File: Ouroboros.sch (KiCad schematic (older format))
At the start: 132 parts, among them J1 E1_3.5mm, J10 E1_3.5mm, J11 E1_3.5mm, J12 PWR_IN_PHNX, J13 PWR_IN_PHNX, J14 PWR_IN_PHNX, J15 PWR_IN_PHNX, J16 E1_3.5mm, J2 E1_3.5mm, J3 E1_3.5mm, J4 E1_3.5mm, J5 E1_3.5mm, J6 E1_3.5mm, J7 E1_3.5mm, J8 E1_3.5mm, J9 E1_3.5mm, SW1 SW_SPDT, U1 CD4017, U10 LM324, U11 LM324, U12 LM324, U13 LM324, U14 LM324, U15 NE555, U2 CD4017, U3 CD4017, U4 CD4017, U5 CD4017, U6 CD4017, U7 CD4017, U8 CD4017, U9 CD4017

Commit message: made schematic
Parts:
- added C?: 0.1uf, symbol Device:C
- added C?: 10uf, Capacitor_THT:CP_Radial_D5.0mm_P2.00mm, symbol Device:CP
- added D? (x19): 1N914, symbol Device:D
- added R? (x11): 10k, HammerheadAudio:R_THT_P7.62, symbol Device:R
- added R?: 10k, symbol Device:R
- added R?: 1k, HammerheadAudio:R_THT_P7.62, symbol Device:R
- added U?: CD4048, symbol CD4048:CD4048
- R24: value 1k -> 10k
- R25: value 220 -> 1k
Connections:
- net ALL: now also D?.2 (A), U?.1 (Out); no longer U12.10 (+)
- net GND: now also C?.2, D?.2 (A), R?.1, R?.2, R?.2, R?.2, R?.2, R?.2, R?.2, R?.2, R?.2, R?.2, R?.2, U?.15 (Exp), U?.7 (Kb), U?.8 (Vss), U?.9 (Kc); no longer U9.15 (RES)
- net TRIG_IN: now also R?.2; no longer U10.3 (+)
- net VCC: now also C?.1, U?.10 (Ka), U?.16 (Vdd)
- net VREF: no longer U12.9 (-)
- net at U15.3 (Q): now also R?.1; no longer J16.3 (Pin_3)
- net B2: now reaches R4.2, R5.2, U10.7
- net at U2.15 (RES): now also D?.2 (A); no longer U2.7 (Q3)
- net at U3.10 (Q4): now also D?.1 (K), D?.1 (K), R?.1; no longer U3.15 (RES)
- net at U4.1 (Q5): now also D?.1 (K), D?.1 (K), R?.1; no longer U4.15 (RES)
- net at U5.15 (RES): now also D?.2 (A); no longer U5.5 (Q6)
- net at U6.15 (RES): now also D?.2 (A); no longer U6.6 (Q7)
- net at U7.15 (RES): now also D?.2 (A); no longer U7.9 (Q8)
- net at U8.11 (Q9): now also D?.1 (K), D?.1 (K), R?.1; no longer U8.15 (RES)
- net B5: now reaches R10.2, R11.2, U11.1
- net B6: now reaches R12.2, R13.2, U11.7
- net B7: now reaches R14.2, R15.2, U11.8
- net B8: now reaches R16.2, R17.2, U11.14
- net B9: now reaches R18.2, R19.2, U12.1
- net B10: now reaches R20.2, R21.2, U12.7
- net B10: now also U?.11 (D), U?.12 (C), U?.13 (B), U?.14 (A), U?.2 (Kd), U?.3 (H), U?.4 (G), U?.5 (F), U?.6 (E)
- net at R22.2, R23.2, U12.8: now also U12.9 (-)
- net B3: now reaches R6.2, R7.2, U10.8
- net B4: now reaches R8.2, R9.2, U10.14
- net at U1.15 (RES): now also D?.2 (A); no longer U1.4 (Q2)
- new net: J16.3 (Pin_3), R?.2
- new net: D?.1 (K), R?.1, U10.3 (+)
- new net: D?.1 (K), D?.1 (K), R?.1, U2.7 (Q3)
- new net: D?.2 (A), U3.15 (RES)
- new net: D?.2 (A), U4.15 (RES)
- new net: D?.1 (K), D?.1 (K), R?.1, U5.5 (Q6)
- new net: D?.1 (K), D?.1 (K), R?.1, U6.6 (Q7)
- new net: D?.1 (K), D?.1 (K), R?.1, U7.9 (Q8)
- new net: D?.2 (A), U8.15 (RES)
- new net: D?.1 (K), R?.1, U9.15 (RES)
- new net: C?.1, D?.1 (K), R?.2, U12.10 (+)
- new net: D?.1 (K), D?.1 (K), R?.1, U1.4 (Q2)
- new net RESET: C?.2, D?.2 (A), D?.2 (A), D?.2 (A), D?.2 (A), D?.2 (A), D?.2 (A), D?.2 (A), D?.2 (A), D?.2 (A), R?.1
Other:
- moved on the sheet: D0, D1, D65, J1, J11, J16, R1, R2, R22, R23, R24, R25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

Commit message: cleaned up schematic errors
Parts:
- added SW2: SW_Push, Button_Switch_THT:SW_PUSH_6mm, symbol Switch:SW_Push
- C4: renamed from C?; footprint (none) -> Capacitor_THT:C_Disc_D3.0mm_W2.0mm_P2.50mm
- D0, D1, D2, D3, D4, D5, D6, D7, D8, D9: footprint (none) -> HammerheadAudio:LED_Centered
- D10, D11, D12, D13, D14, D15, D16, D17, D18, D19, D20, D21, D22, D23, D24, D25, D26, D27, D28, D29, D30, D31, D32, D33, D34, D35, D36, D37, D38, D39, D40, D41, D42, D43, D44, D45, D46, D47, D48, D49, D50, D51, D52, D53, D54, D55, D56, D57, D58, D59, D60, D61, D62, D63, D64, D65: footprint (none) -> HammerheadAudio:LED_Centered_NoRef
- D68, D69, D70, D71, D72, D73, D74, D75, D76, D77, D78, D79, D80, D81, D82, D83, D84, D85, D86: renamed from D?; footprint (none) -> HammerheadAudio:DO-35-P5mm
- R29: renamed from R?; footprint (none) -> HammerheadAudio:R_THT_P7.62
- U16: renamed from U?; footprint (none) -> Package_DIP:DIP-16_W7.62mm_Socket
- gave numbers to parts that had none: 13
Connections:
- net B10: no longer U16.11 (D), U16.12 (C), U16.13 (B), U16.14 (A), U16.3 (H), U16.4 (G), U16.5 (F), U16.6 (E)
- net B2: now also U16.11 (D)
- net B3: now also U16.12 (C)
- net B4: now also U16.13 (B)
- net B5: now also U16.14 (A)
- net B6: now also U16.6 (E)
- net B7: now also U16.5 (F)
- net B8: now also U16.4 (G)
- net B9: now also U16.3 (H)
- net DIV10: now also D55.2 (A), U9.3 (Q0)
- net DIV9: no longer D55.2 (A), U9.3 (Q0)
- net GND: now also D11.1 (K)
- net RESET: now also SW2.1
- net VCC: now also SW2.2
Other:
- moved on the sheet: C4, R40

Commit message: cleaned up schematic errors
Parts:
- removed C3: 10uf, Capacitor_THT:CP_Radial_D5.0mm_P2.00mm, symbol Device:CP
- D10: footprint HammerheadAudio:LED_Centered_NoRef -> HammerheadAudio:LED_Centered
- renumbered C4 to C3, C5 to C4, U13 to U11, U14 to U12, U16 to U13, U15 to U14
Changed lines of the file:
@@
 F 0 "D10" H 2493 9445 50  0000 C CNN
 F 1 "LED" H 2493 9536 50  0000 C CNN
-F 2 "HammerheadAudio:LED_Centered_NoRef" H 2500 9700 50  0001 C CNN
+F 2 "HammerheadAudio:LED_Centered" H 2500 9700 50  0001 C CNN
 F 3 "~" H 2500 9700 50  0001 C CNN
 	1    2500 9700
@@
 	950  12650 1000 12650
 $Comp
-L Timer:NE555 U15
+L Timer:NE555 U14
 U 1 1 5E794E13
 P 15650 5550
-F 0 "U15" H 15350 5900 50  0000 C CNN
+F 0 "U14" H 15350 5900 50  0000 C CNN
 F 1 "NE555" H 15900 5900 50  0000 C CNN
 F 2 "Package_DIP:DIP-8_W7.62mm_Socket" H 15650 5550 50  0001 C CNN
@@
 	16150 5750 16150 6100
 Wire Wire Line
-	16150 6300 15250 6300
-Wire Wire Line
 	14850 6300 14850 5350
 Wire Wire Line
@@
 $EndComp
 $Comp
-L Amplifier_Operational:LM324 U13
+L Amplifier_Operational:LM324 U11
 U 5 1 5EA7F911
 P 14900 2000
-F 0 "U13" H 14858 2046 50  0000 L CNN
+F 0 "U11" H 14858 2046 50  0000 L CNN
 F 1 "LM324" H 14858 1955 50  0000 L CNN
 F 2 "Package_DIP:DIP-14_W7.62mm_Socket" H 14850 2100 50  0001 C CNN
@@
 	14400 3750 14650 3750
 $Comp
-L Amplifier_Operational:LM324 U14
+L Amplifier_Operational:LM324 U12
 U 5 1 5E8E8FA2
 P 15350 2000
-F 0 "U14" H 15308 2046 50  0000 L CNN
+F 0 "U12" H 15308 2046 50  0000 L CNN
 F 1 "LM324" H 15308 1955 50  0000 L CNN
 F 2 "Package_DIP:DIP-14_W7.62mm_Socket" H 15300 2100 50  0001 C CNN
@@
 Wire Wire Line
 	15250 2400 15250 2450
-$Comp
-L Device:CP C3
-U 1 1 5E7E848A
-P 15250 6500
-F 0 "C3" H 15368 6546 50  0000 L CNN
-F 1 "10uf" H 15368 6455 50  0000 L CNN
-F 2 "Capacitor_THT:CP_Radial_D5.0mm_P2.00mm" H 15288 6350 50  0001 C CNN
-F 3 "~" H 15250 6500 50  0001 C CNN
-	1    15250 6500
-	1    0    0    -1
-$EndComp
-Wire Wire Line
-	15250 6350 15250 6300
-Connection ~ 15250 6300
-Wire Wire Line
-	15250 6300 14850 6300
-Wire Wire Line
-	14850 6650 14850 6700
-Wire Wire Line
-	15250 6650 15250 6700
-Wire Wire Line
-	15250 6700 14850 6700
-Connection ~ 14850 6700
-Wire Wire Line
-	14850 6700 14850 6750
 Wire Wire Line
 	16150 5350 16550 5350
@@
 	5250 8600 5250 8550
 $Comp
-L Device:C C4
+L Device:C C3
 U 1 1 6155F9DF
 P 5250 7950
-F 0 "C4" H 5365 7996 50  0000 L CNN
+F 0 "C3" H 5365 7996 50  0000 L CNN
 F 1 "0.1uf" H 5365 7905 50  0000 L CNN
 F 2 "Capacitor_THT:C_Disc_D3.0mm_W2.0mm_P2.50mm" H 5288 7800 50  0001 C CNN
@@
 	16950 5350 16850 5350
 $Comp
-L CD4048:CD4048 U16
+L CD4048:CD4048 U13
 U 1 1 61A5E271
 P 8650 8300
-F 0 "U16" H 8650 8565 50  0000 C CNN
+F 0 "U13" H 8650 8565 50  0000 C CNN
 F 1 "CD4048" H 8650 8474 50  0000 C CNN
 F 2 "Package_DIP:DIP-16_W7.62mm_Socket" H 8150 8300 50  0001 C CNN
@@
 $EndComp
 $Comp
-L Device:CP C5
+L Device:CP C4
 U 1 1 624F28D9
 P 1400 10950
-F 0 "C5" H 1518 10996 50  0000 L CNN
+F 0 "C4" H 1518 10996 50  0000 L CNN
 F 1 "10uf" H 1518 10905 50  0000 L CNN
 F 2 "Capacitor_THT:CP_Radial_D5.0mm_P2.00mm" H 1438 10800 50  0001 C CNN
@@
 Wire Wire Line
 	1200 9250 1250 9250
+Wire Wire Line
+	14850 6650 14850 6750
+Wire Wire Line
+	14850 6300 16150 6300
 $EndSCHEMATC

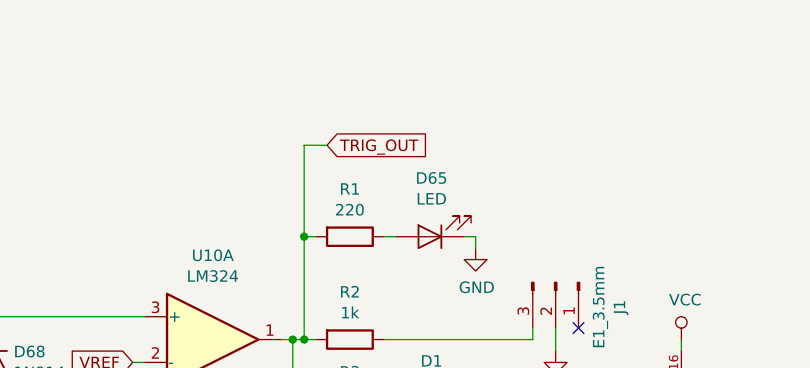
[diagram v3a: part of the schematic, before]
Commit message: added clock in indicator led
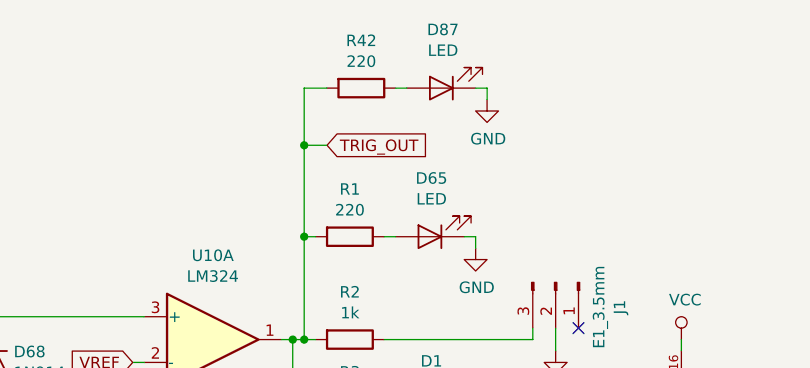
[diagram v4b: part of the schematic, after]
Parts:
- added D87: LED, HammerheadAudio:LED_Centered_NoRef, symbol Device:LED
- added R42: 220, HammerheadAudio:R_THT_P7.62, symbol Device:R
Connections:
- net GND: now also D87.1 (K)
- net TRIG_OUT: now also R42.2
- new net: D87.2 (A), R42.1
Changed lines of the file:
@@
 Wire Wire Line
 	14850 6300 16150 6300
+$Comp
+L Device:LED D87
+U 1 1 5F384FB5
+P 3250 300
+F 0 "D87" H 3243 45  50  0000 C CNN
+F 1 "LED" H 3243 136 50  0000 C CNN
+F 2 "HammerheadAudio:LED_Centered_NoRef" H 3250 300 50  0001 C CNN
+F 3 "~" H 3250 300 50  0001 C CNN
+	1    3250 300
+	-1   0    0    1
+$EndComp
+$Comp
+L power:GND #PWR0119
+U 1 1 5F384FBF
+P 3450 350
+F 0 "#PWR0119" H 3450 100 50  0001 C CNN
+F 1 "GND" H 3455 177 50  0000 C CNN
+F 2 "" H 3450 350 50  0001 C CNN
+F 3 "" H 3450 350 50  0001 C CNN
+	1    3450 350
+	1    0    0    -1
+$EndComp
+Wire Wire Line
+	3050 300  3100 300
+Wire Wire Line
+	3450 350  3450 300
+Wire Wire Line
+	3450 300  3400 300
+$Comp
+L Device:R R42
+U 1 1 5F384FCC
+P 2900 300
+F 0 "R42" V 2693 300 50  0000 C CNN
+F 1 "220" V 2784 300 50  0000 C CNN
+F 2 "HammerheadAudio:R_THT_P7.62" V 2830 300 50  0001 C CNN
+F 3 "~" H 2900 300 50  0001 C CNN
+	1    2900 300
+	0    1    1    0
+$EndComp
+Wire Wire Line
+	2650 550  2650 300
+Wire Wire Line
+	2650 300  2750 300
+Connection ~ 2650 550
 $EndSCHEMATC

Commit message: organized components'
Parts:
- added R43: 10k, HammerheadAudio:R_THT_P7.62, symbol Device:R
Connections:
- net at D68.1 (K), R29.1: now also R43.2; no longer U10.3 (+)
- net at U2.15 (RES): now also D70.1 (K), D73.1 (K), R31.1; no longer D73.2 (A)
- net at D71.1 (K), D74.1 (K), R32.1: now also U3.15 (RES); no longer U3.10 (Q4)
- net at D74.2 (A): now also U3.10 (Q4); no longer U3.15 (RES)
- net at D75.1 (K), D78.1 (K), R33.1: now also U4.15 (RES); no longer U4.1 (Q5)
- net at D78.2 (A): now also U4.1 (Q5); no longer U4.15 (RES)
- net at U5.15 (RES): now also D76.1 (K), D79.1 (K), R34.1; no longer D79.2 (A)
- net at U6.15 (RES): now also D77.1 (K), D80.1 (K), R35.1; no longer D80.2 (A)
- net at U7.15 (RES): now also D81.1 (K), D83.1 (K), R37.1; no longer D83.2 (A)
- net at D82.1 (K), D84.1 (K), R38.1: now also U8.15 (RES); no longer U8.11 (Q9)
- net at D84.2 (A): now also U8.11 (Q9); no longer U8.15 (RES)
- net at U1.15 (RES): now also D69.1 (K), D72.1 (K), R30.1; no longer D72.2 (A)
- new net: R43.1, U10.3 (+)
- new net: D73.2 (A), U2.7 (Q3)
- new net: D79.2 (A), U5.5 (Q6)
- new net: D80.2 (A), U6.6 (Q7)
- new net: D83.2 (A), U7.9 (Q8)
- new net: D72.2 (A), U1.4 (Q2)
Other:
- moved on the sheet: D69, D70, D71, D75, D76, D77, D81, D82, R30, R31, R32, R33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
